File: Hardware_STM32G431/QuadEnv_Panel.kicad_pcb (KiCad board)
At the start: 2 copper layers, 20.3 x 128.5 mm, 14 parts

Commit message: Started creating firmware for STM32G431
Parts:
- added G***: LOGO, Graphics:Env_logo, B.Cu at (54.3, 39.9)
- added Ge: LOGO, Graphics:Quad_logo, B.Cu at (54.6, 36.8)
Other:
- board text added: "Mountjoy Modular"

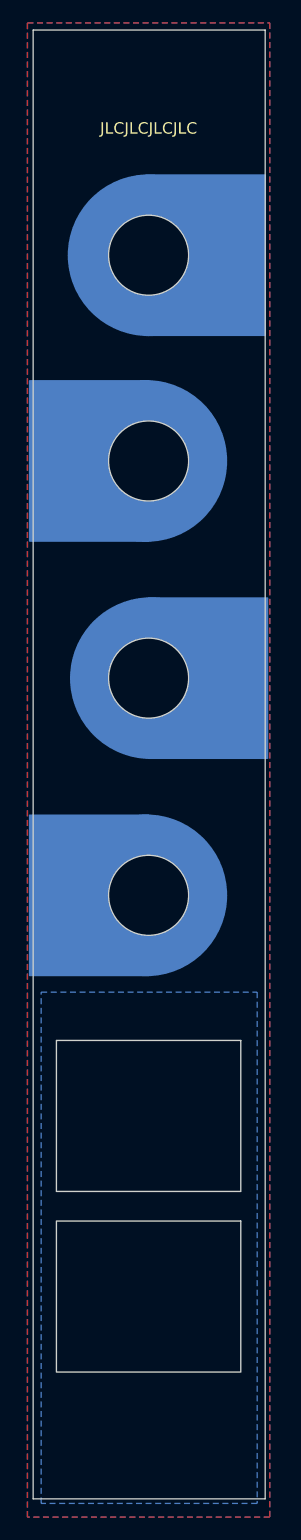
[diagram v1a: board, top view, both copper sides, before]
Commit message: Added PWM Test code
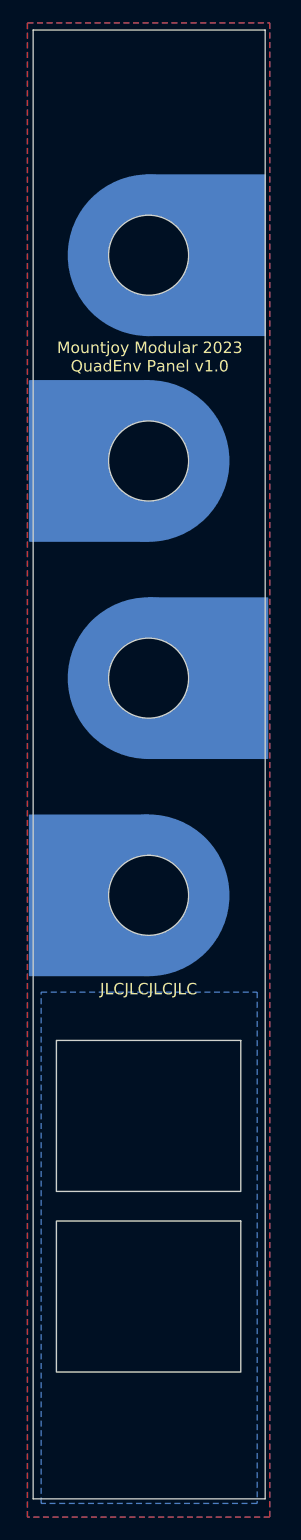
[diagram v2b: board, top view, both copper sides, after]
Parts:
- moved kibuzzard-640B6CC5 0.25 mm to (65.4, 50.5)
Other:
- board text added: "Mountjoy Modular 2023 QuadEnv Panel v1.0"
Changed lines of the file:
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@@
       (outputformat 1)
       (mirror false)
-      (drillshape 1)
+      (drillshape 0)
       (scaleselection 1)
-      (outputdirectory "")
+      (outputdirectory "Gerbers/QuadEnv_Panel/")
     )
   )
@@
     (fp_circle (center 0 0) (end 6 0) (layer "B.CrtYd") (width 0.05) (fill none))
     (pad "" np_thru_hole circle (at 0 0 180) (size 7 7) (drill 7) (layers F&B.Cu *.Mask))
-    (model "${CUSTOM_3D}/Sifam_Knob_Small_Tall_Unskirted.step"
+    (model "${CUSTOM_3D}/Sifam_Knob_Small_Unskirted.step"
       (offset (xyz 0 0 0))
       (scale (xyz 1 1 1))
@@
   )
   (footprint "kibuzzard-640B6CC5" (layer "B.Cu")
-    (at 65.15 50.5 180)
+    (at 65.4 50.5 180)
     (descr "Generated with KiBuzzard")
     (tags "kb_params=eyJBbGlnbm1lbnRDaG9pY2UiOiAiQ2VudGVyIiwgIkNhcExlZnRDaG9pY2UiOiAiWyIsICJDYXBSaWdodENob2ljZSI6ICIvIiwgIkZvbnRDb21ib0JveCI6ICJSb2JvdG8tQm9sZCIsICJIZWlnaHRDdHJsIjogIjIuNSIsICJMYXllckNvbWJvQm94IjogIkYuTWFzayIsICJNdWx0aUxpbmVUZXh0IjogIkEiLCAiUGFkZGluZ0JvdHRvbUN0cmwiOiAiMyIsICJQYWRkaW5nTGVmdEN0cmwiOiAiMTAiLCAiUGFkZGluZ1JpZ2h0Q3RybCI6ICIyMCIsICJQYWRkaW5nVG9wQ3RybCI6ICIzIiwgIldpZHRoQ3RybCI6ICIifQ==")
@@
     (fp_circle (center 0 0) (end 6 0) (layer "B.CrtYd") (width 0.05) (fill none))
     (pad "" np_thru_hole circle (at 0 0 180) (size 7 7) (drill 7) (layers F&B.Cu *.Mask))
-    (model "${CUSTOM_3D}/Sifam_Knob_Small_Tall_Unskirted.step"
+    (model "${CUSTOM_3D}/Sifam_Knob_Small_Unskirted.step"
       (offset (xyz 0 0 0))
       (scale (xyz 1 1 1))
@@
     (fp_circle (center 0 0) (end 6 0) (layer "B.CrtYd") (width 0.05) (fill none))
     (pad "" np_thru_hole circle (at 0 0 180) (size 7 7) (drill 7) (layers *.Cu *.Mask))
-    (model "${CUSTOM_3D}/Sifam_Knob_Small_Tall_Unskirted.step"
+    (model "${CUSTOM_3D}/Sifam_Knob_Small_Unskirted.step"
       (offset (xyz 0 0 0))
       (scale (xyz 1 1 1))
@@
     (fp_circle (center 0 0) (end 6 0) (layer "B.CrtYd") (width 0.05) (fill none))
     (pad "" np_thru_hole circle (at 0 0 180) (size 7 7) (drill 7) (layers F&B.Cu *.Mask))
-    (model "${CUSTOM_3D}/Sifam_Knob_Small_Tall_Unskirted.step"
+    (model "${CUSTOM_3D}/Sifam_Knob_Small_Unskirted.step"
       (offset (xyz 0 0 0))
       (scale (xyz 1 1 1))
@@
   (gr_rect (start 69.8 84) (end 59.4 98) (layer "B.Cu") (width 0.15) (fill solid))
   (gr_circle (center 59.4 54) (end 66.4 54) (layer "B.Cu") (width 0.15) (fill solid))
-  (gr_circle (center 59.2 110) (end 52.2 110) (layer "B.Cu") (width 0.15) (fill solid))
-  (gr_circle (center 59.2 72) (end 52.2 72) (layer "B.Cu") (width 0.15) (fill solid))
-  (gr_circle (center 59.6 91) (end 66.6 91) (layer "B.Cu") (width 0.15) (fill solid))
+  (gr_circle (center 59.4 110) (end 52.4 110) (layer "B.Cu") (width 0.15) (fill solid))
+  (gr_circle (center 59.4 72) (end 52.4 72) (layer "B.Cu") (width 0.15) (fill solid))
+  (gr_circle (center 59.4 91) (end 66.4 91) (layer "B.Cu") (width 0.15) (fill solid))
   (gr_rect (start 49 79) (end 59.4 65) (layer "B.Cu") (width 0.15) (fill solid))
   (gr_rect (start 69.6 47) (end 59.2 61) (layer "B.Cu") (width 0.15) (fill solid))
@@
   (gr_line locked (start 59.4 48.3) (end 59.4 161.5) (layer "Dwgs.User") (width 0.15))
   (gr_rect locked (start 49.3 34.3) (end 69.6 162.8) (layer "Edge.Cuts") (width 0.1) (fill none))
-  (gr_text "JLCJLCJLCJLC" (at 59.4 42.9) (layer "F.SilkS")
+  (gr_text "JLCJLCJLCJLC" (at 59.4 118.2) (layer "F.SilkS")
     (effects (font (size 1 1) (thickness 0.15)))
   )
+  (gr_text "Mountjoy Modular 2023\nQuadEnv Panel v1.0" (at 59.5 62.9) (layer "F.SilkS")
+    (effects (font (size 1 1) (thickness 0.15)))
+  )

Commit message: Clean up project for manufacture
Fixed LED ordering bug on control board
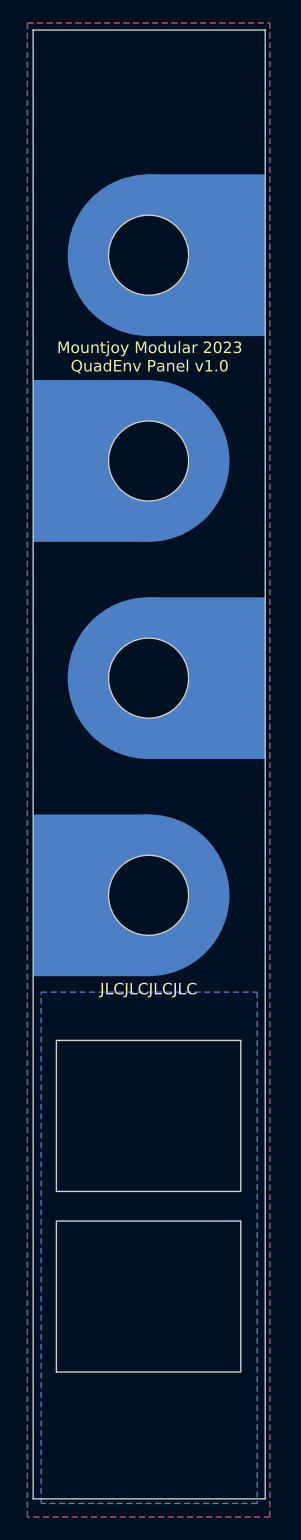
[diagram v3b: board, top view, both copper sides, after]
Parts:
- removed kibuzzard-640B6B46: G***, kibuzzard-640B6B46
- removed kibuzzard-640B6B56: G***, kibuzzard-640B6B56
- added kibuzzard-64244971: G***, kibuzzard-64244971, B.Cu at (58.3, 153.3)
- added kibuzzard-6424498C: G***, kibuzzard-6424498C, B.Cu at (61.0, 121.2)
- turned REF** to 0 degrees
